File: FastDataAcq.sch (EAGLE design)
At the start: 224 parts, among them IC1 LT1963AEQ, IC2 FT230XQ, IC3 ADCMP553BRMZ, J1 MICRO-FIT_3.0_2POS_RA_SMD, J2 USB_MICROAB_SMT, X1 87832-14, X2 SMA-142-0701-801/806, X3 SMA-142-0701-801/806, Y1 SI530-500, Y2 100MHz, Y3 DNP

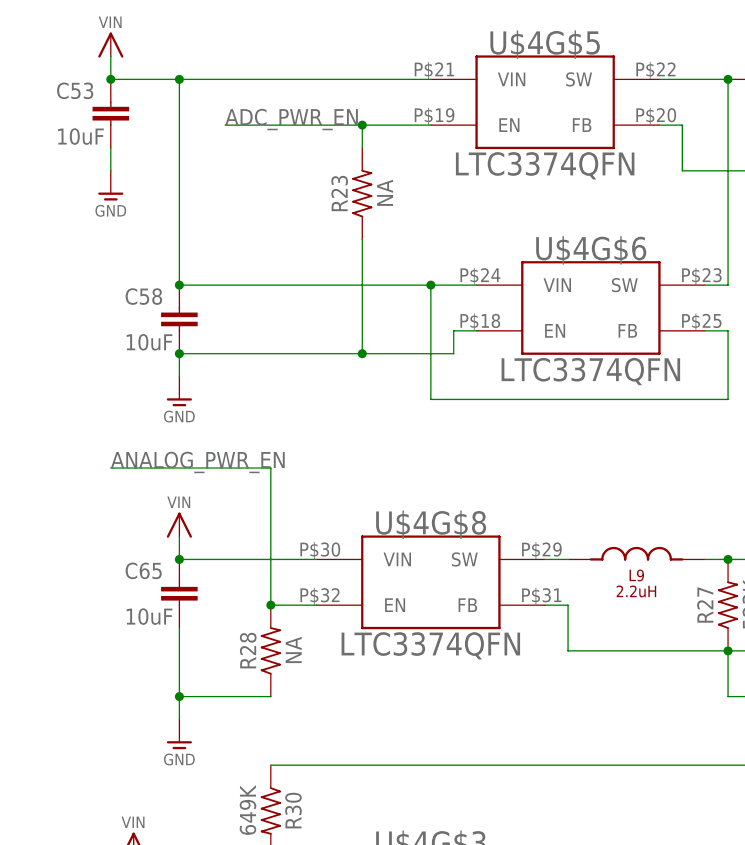
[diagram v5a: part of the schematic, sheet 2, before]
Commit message: Board layout almost complete.
Power plane almost routes all the power correctly.
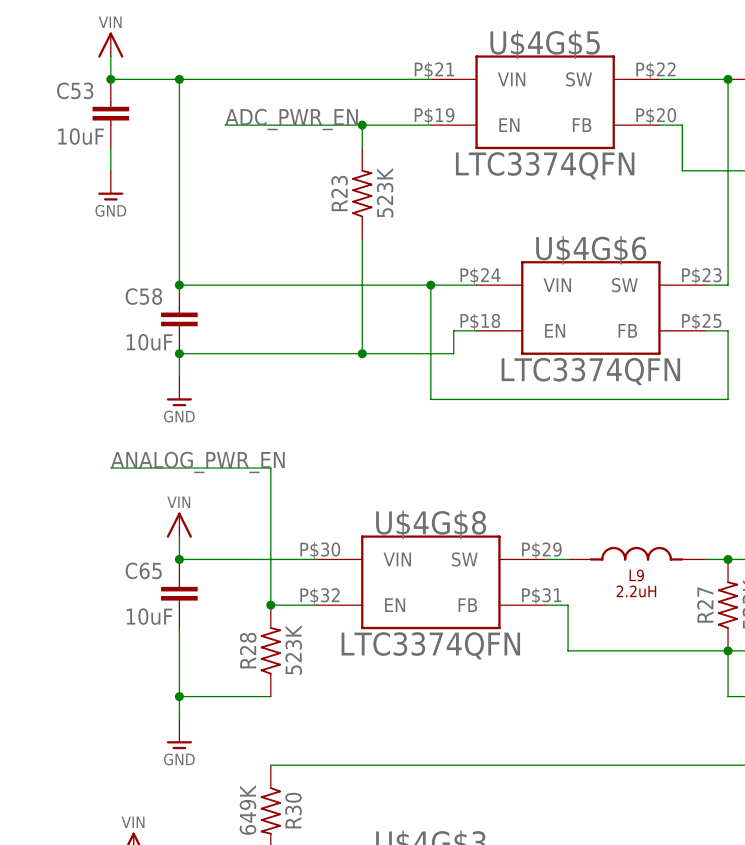
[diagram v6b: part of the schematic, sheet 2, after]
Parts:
- R23, R28: value NA -> 523K; device rcl:R-US_R0603 -> rcl:R-US_R0201; PARTNUMBER (none) -> P523KABCT-ND; SUPPLIER (none) -> DIGIKEY
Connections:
- net N$6 renamed S_MODE
- net S4EN renamed S3EN
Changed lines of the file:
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@@
 <attribute name="SUPPLIER" value=""/>
 </part>
-<part name="R28" library="rcl" deviceset="R-US_" device="R0603" value="NA">
-<attribute name="MANPARTNUMBER" value=""/>
-<attribute name="MANUFACTURER" value=""/>
-<attribute name="PARTNUMBER" value=""/>
-<attribute name="SUPPLIER" value=""/>
-</part>
-<part name="R23" library="rcl" deviceset="R-US_" device="R0603" value="NA">
-<attribute name="MANPARTNUMBER" value=""/>
-<attribute name="MANUFACTURER" value=""/>
-<attribute name="PARTNUMBER" value=""/>
-<attribute name="SUPPLIER" value=""/>
-</part>
 <part name="C7" library="rcl" deviceset="C-EU" device="C0603" value="NA">
 <attribute name="PARTNUMBER" value=""/>
@@
 <part name="S1" library="Schuyler" deviceset="SLIDER_SPDT" device="_AYZ0102AGRLC"/>
 <part name="SUPPLY1" library="Schuyler" deviceset="SUP_VIN" device="" value="Vin"/>
+<part name="R23" library="rcl" deviceset="R-US_" device="R0201" value="523K">
+<attribute name="PARTNUMBER" value="P523KABCT-ND"/>
+<attribute name="SUPPLIER" value="DIGIKEY"/>
+</part>
+<part name="R28" library="rcl" deviceset="R-US_" device="R0201" value="523K">
+<attribute name="PARTNUMBER" value="P523KABCT-ND"/>
+<attribute name="SUPPLIER" value="DIGIKEY"/>
+</part>
 </parts>
 <sheets>
@@
 <attribute name="SUPPLIER" x="22.86" y="17.78" size="1.778" layer="96" display="off"/>
 </instance>
-<instance part="R28" gate="G$1" x="33.02" y="50.8" rot="R90">
-<attribute name="MANPARTNUMBER" x="33.02" y="50.8" size="1.778" layer="96" rot="R90" display="off"/>
-<attribute name="MANUFACTURER" x="33.02" y="50.8" size="1.778" layer="96" rot="R90" display="off"/>
-<attribute name="PARTNUMBER" x="33.02" y="50.8" size="1.778" layer="96" rot="R90" display="off"/>
-<attribute name="SUPPLIER" x="33.02" y="50.8" size="1.778" layer="96" rot="R90" display="off"/>
-</instance>
-<instance part="R23" gate="G$1" x="43.18" y="101.6" rot="R90">
-<attribute name="MANPARTNUMBER" x="43.18" y="101.6" size="1.778" layer="96" rot="R90" display="off"/>
-<attribute name="MANUFACTURER" x="43.18" y="101.6" size="1.778" layer="96" rot="R90" display="off"/>
-<attribute name="PARTNUMBER" x="43.18" y="101.6" size="1.778" layer="96" rot="R90" display="off"/>
-<attribute name="SUPPLIER" x="43.18" y="101.6" size="1.778" layer="96" rot="R90" display="off"/>
-</instance>
 <instance part="C7" gate="G$1" x="157.48" y="210.82">
 <attribute name="PARTNUMBER" x="157.48" y="210.82" size="1.778" layer="96" display="off"/>
@@
 <instance part="S1" gate="G$1" x="25.4" y="193.04" rot="R90"/>
 <instance part="SUPPLY1" gate="G$1" x="43.18" y="203.2"/>
+<instance part="R23" gate="G$1" x="43.18" y="101.6" rot="R90">
+<attribute name="PARTNUMBER" x="43.18" y="101.6" size="1.778" layer="96" rot="R90" display="off"/>
+<attribute name="SUPPLIER" x="43.18" y="101.6" size="1.778" layer="96" rot="R90" display="off"/>
+</instance>
+<instance part="R28" gate="G$1" x="33.02" y="50.8" rot="R90">
+<attribute name="PARTNUMBER" x="33.02" y="50.8" size="1.778" layer="96" rot="R90" display="off"/>
+<attribute name="SUPPLIER" x="33.02" y="50.8" size="1.778" layer="96" rot="R90" display="off"/>
+</instance>
 </instances>
 <busses>
@@
 </segment>
 </net>
-<net name="N$6" class="0">
+<net name="S_MODE" class="0">
 <segment>
 <pinref part="U$4" gate="G$9" pin="MODE"/>
@@
 <wire x1="50.8" y1="109.22" x2="43.18" y2="109.22" width="0.1524" layer="91"/>
 <label x="27.94" y="109.22" size="1.778" layer="95"/>
-<pinref part="R23" gate="G$1" pin="2"/>
 <wire x1="43.18" y1="109.22" x2="27.94" y2="109.22" width="0.1524" layer="91"/>
 <wire x1="43.18" y1="106.68" x2="43.18" y2="109.22" width="0.1524" layer="91"/>
 <junction x="43.18" y="109.22"/>
+<pinref part="R23" gate="G$1" pin="2"/>
 </segment>
 </net>
@@
 </segment>
 </net>
-<net name="S4EN" class="0">
+<net name="S3EN" class="0">
 <segment>
 <pinref part="U$4" gate="G$3" pin="EN"/>
@@
 <pinref part="U$4" gate="G$6" pin="EN"/>
 <wire x1="53.34" y1="86.36" x2="55.88" y2="86.36" width="0.1524" layer="91"/>
-<pinref part="R23" gate="G$1" pin="1"/>
 <wire x1="43.18" y1="96.52" x2="43.18" y2="83.82" width="0.1524" layer="91"/>
 <junction x="43.18" y="83.82"/>
 <pinref part="U$61" gate="G$1" pin="GND"/>
+<pinref part="R23" gate="G$1" pin="1"/>
 </segment>
 <segment>
@@
 <wire x1="33.02" y1="45.72" x2="22.86" y2="45.72" width="0.1524" layer="91"/>
 <junction x="22.86" y="45.72"/>
-<pinref part="R28" gate="G$1" pin="1"/>
 <pinref part="U$63" gate="G$1" pin="GND"/>
+<pinref part="R28" gate="G$1" pin="1"/>
 </segment>
 <segment>

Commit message: Continued board layout
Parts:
- removed JP2: JUMPER-2PTH, SparkFun-Passives:JUMPER-2PTH
- removed JP3: M10", SparkFun-Connectors:M10"
- added J3: HEADER_0.1"_10P_2R_SMT, Schuyler:HEADER_0.1"_10P_2R_SMT
- added R40: 0, rcl:R-US_R0603
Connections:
- net 3V3: now also J3.P$1; no longer JP3.10
- net FPGA_GPIO1: now also J3.P$9; no longer JP3.2
- net FPGA_GPIO2: now also J3.P$8; no longer JP3.3
- net FPGA_GPIO3: now also J3.P$7; no longer JP3.4
- net FPGA_GPIO4: now also J3.P$6; no longer JP3.5
- net FPGA_GPIO5: now also J3.P$5; no longer JP3.6
- net FPGA_GPIO6: now also J3.P$4; no longer JP3.7
- net FPGA_GPIO7: now also J3.P$3; no longer JP3.8
- net GND: now also J3.P$2; no longer JP3.9
- net S_MODE: now also R40.2; no longer JP2.1
- net VIN: now also R40.1; no longer JP2.2
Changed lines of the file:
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@@
 <part name="TP3" library="testpad" deviceset="TP" device="PAD1-13"/>
 <part name="SUPPLY53" library="Schuyler" deviceset="SUP_VIN" device="" value="Vin"/>
-<part name="JP2" library="SparkFun-Passives" deviceset="JUMPER-2" device="PTH"/>
 <part name="SUPPLY74" library="Schuyler" deviceset="SUP_VIN" device="" value="Vin"/>
 <part name="R7" library="rcl" deviceset="R-US_" device="R0201" value="4.7k">
@@
 <part name="D3" library="Schuyler" deviceset="LED_" device="0603_GREEN"/>
 <part name="D4" library="Schuyler" deviceset="LED_" device="0603_RED"/>
-<part name="JP3" library="SparkFun-Connectors" deviceset="M10" device="&quot;"/>
 <part name="R42" library="rcl" deviceset="R-US_" device="R0201" value="330">
 <attribute name="MANPARTNUMBER" value="RC0603J331CS"/>
@@
 <attribute name="SUPPLIER" value="DIGIKEY"/>
 </part>
+<part name="R40" library="rcl" deviceset="R-US_" device="R0603" value="0">
+<attribute name="PARTNUMBER" value="311-0.0GRCT-ND"/>
+<attribute name="SUPPLIER" value="DIGIKEY"/>
+</part>
+<part name="J3" library="Schuyler" deviceset="HEADER_0.1&quot;_" device="10P_2R_SMT"/>
 </parts>
 <sheets>
@@
 <instance part="TP3" gate="G$1" x="251.46" y="223.52"/>
 <instance part="SUPPLY53" gate="G$1" x="109.22" y="220.98"/>
-<instance part="JP2" gate="A" x="116.84" y="228.6"/>
-<instance part="SUPPLY74" gate="G$1" x="124.46" y="228.6"/>
+<instance part="SUPPLY74" gate="G$1" x="127" y="228.6"/>
 <instance part="IC1" gate="A" x="165.1" y="106.68">
 <attribute name="MANPARTNUMBER" x="165.1" y="106.68" size="1.778" layer="96" display="off"/>
@@
 <attribute name="SUPPLIER" x="33.02" y="50.8" size="1.778" layer="96" rot="R90" display="off"/>
 </instance>
+<instance part="R40" gate="G$1" x="121.92" y="226.06" rot="R180">
+<attribute name="PARTNUMBER" x="121.92" y="226.06" size="1.778" layer="96" rot="R180" align="bottom-right" display="off"/>
+<attribute name="SUPPLIER" x="121.92" y="226.06" size="1.778" layer="96" rot="R180" align="bottom-right" display="off"/>
+</instance>
 </instances>
 <busses>
@@
 </segment>
 <segment>
-<pinref part="JP2" gate="A" pin="2"/>
 <pinref part="SUPPLY74" gate="G$1" pin="VIN"/>
-<wire x1="119.38" y1="226.06" x2="124.46" y2="226.06" width="0.1524" layer="91"/>
-<wire x1="124.46" y1="226.06" x2="124.46" y2="228.6" width="0.1524" layer="91"/>
+<wire x1="127" y1="226.06" x2="127" y2="228.6" width="0.1524" layer="91"/>
+<pinref part="R40" gate="G$1" pin="1"/>
 </segment>
 <segment>
@@
 <segment>
 <pinref part="U$4" gate="G$9" pin="MODE"/>
-<pinref part="JP2" gate="A" pin="1"/>
 <wire x1="104.14" y1="226.06" x2="116.84" y2="226.06" width="0.1524" layer="91"/>
 <wire x1="116.84" y1="226.06" x2="116.84" y2="223.52" width="0.1524" layer="91"/>
-<junction x="116.84" y="226.06"/>
 <pinref part="R18" gate="G$1" pin="2"/>
+<pinref part="R40" gate="G$1" pin="2"/>
+<junction x="116.84" y="226.06"/>
 </segment>
 </net>
@@
 <instance part="D3" gate="G$1" x="228.6" y="152.4"/>
 <instance part="D4" gate="G$1" x="238.76" y="152.4"/>
-<instance part="JP3" gate="G$1" x="172.72" y="162.56"/>
 <instance part="R42" gate="G$1" x="218.44" y="165.1" rot="R270">
 <attribute name="MANPARTNUMBER" x="218.44" y="165.1" size="1.778" layer="96" rot="R270" display="off"/>
@@
 <instance part="U$88" gate="G$1" x="55.88" y="149.86"/>
 <instance part="U$89" gate="G$1" x="210.82" y="165.1"/>
+<instance part="J3" gate="G$1" x="175.26" y="154.94"/>
 </instances>
 <busses>
@@
 <wire x1="210.82" y1="172.72" x2="210.82" y2="170.18" width="0.1524" layer="91"/>
 <label x="210.82" y="170.18" size="1.778" layer="95"/>
-<pinref part="JP3" gate="G$1" pin="10"/>
 <wire x1="210.82" y1="170.18" x2="210.82" y2="167.64" width="0.1524" layer="91"/>
 <wire x1="210.82" y1="167.64" x2="182.88" y2="167.64" width="0.1524" layer="91"/>
@@
 <label x="182.88" y="167.64" size="1.778" layer="95"/>
 <pinref part="U$21" gate="G$1" pin="3V3"/>
+<pinref part="J3" gate="G$1" pin="P$1"/>
 </segment>
 </net>
@@
 <wire x1="218.44" y1="149.86" x2="205.74" y2="149.86" width="0.1524" layer="91"/>
 <wire x1="205.74" y1="149.86" x2="205.74" y2="162.56" width="0.1524" layer="91"/>
-<pinref part="JP3" gate="G$1" pin="8"/>
 <wire x1="205.74" y1="162.56" x2="182.88" y2="162.56" width="0.1524" layer="91"/>
 <label x="182.88" y="162.56" size="1.778" layer="95"/>
+<pinref part="J3" gate="G$1" pin="P$3"/>
 </segment>
 </net>
 <net name="FPGA_GPIO6" class="0">
 <segment>
-<pinref part="JP3" gate="G$1" pin="7"/>
 <wire x1="182.88" y1="160.02" x2="203.2" y2="160.02" width="0.1524" layer="91"/>
 <wire x1="203.2" y1="160.02" x2="203.2" y2="147.32" width="0.1524" layer="91"/>
@@
 <wire x1="228.6" y1="147.32" x2="228.6" y2="149.86" width="0.1524" layer="91"/>
 <label x="182.88" y="160.02" size="1.778" layer="95"/>
+<pinref part="J3" gate="G$1" pin="P$4"/>
 </segment>
 </net>
@@
 <wire x1="238.76" y1="144.78" x2="200.66" y2="144.78" width="0.1524" layer="91"/>
 <wire x1="200.66" y1="144.78" x2="200.66" y2="157.48" width="0.1524" layer="91"/>
-<pinref part="JP3" gate="G$1" pin="6"/>
 <wire x1="200.66" y1="157.48" x2="182.88" y2="157.48" width="0.1524" layer="91"/>
 <label x="182.88" y="157.48" size="1.778" layer="95"/>
+<pinref part="J3" gate="G$1" pin="P$5"/>
 </segment>
 </net>
 <net name="FPGA_GPIO4" class="0">
 <segment>
-<pinref part="JP3" gate="G$1" pin="5"/>
 <wire x1="182.88" y1="154.94" x2="195.58" y2="154.94" width="0.1524" layer="91"/>
 <label x="182.88" y="154.94" size="1.778" layer="95"/>
+<pinref part="J3" gate="G$1" pin="P$6"/>
 </segment>
 </net>
 <net name="FPGA_GPIO3" class="0">
 <segment>
-<pinref part="JP3" gate="G$1" pin="4"/>
 <wire x1="182.88" y1="152.4" x2="195.58" y2="152.4" width="0.1524" layer="91"/>
 <label x="182.88" y="152.4" size="1.778" layer="95"/>
+<pinref part="J3" gate="G$1" pin="P$7"/>
 </segment>
 </net>
 <net name="FPGA_GPIO2" class="0">
 <segment>
-<pinref part="JP3" gate="G$1" pin="3"/>
 <wire x1="182.88" y1="149.86" x2="195.58" y2="149.86" width="0.1524" layer="91"/>
 <label x="182.88" y="149.86" size="1.778" layer="95"/>
+<pinref part="J3" gate="G$1" pin="P$8"/>
 </segment>
 </net>
 <net name="FPGA_GPIO1" class="0">
 <segment>
-<pinref part="JP3" gate="G$1" pin="2"/>
 <wire x1="182.88" y1="147.32" x2="195.58" y2="147.32" width="0.1524" layer="91"/>
 <label x="182.88" y="147.32" size="1.778" layer="95"/>
+<pinref part="J3" gate="G$1" pin="P$9"/>
 </segment>
 </net>
@@
 </segment>
 <segment>
-<pinref part="JP3" gate="G$1" pin="9"/>
 <wire x1="182.88" y1="165.1" x2="210.82" y2="165.1" width="0.1524" layer="91"/>
 <label x="182.88" y="165.1" size="1.778" layer="95"/>
 <pinref part="U$89" gate="G$1" pin="GND"/>
+<pinref part="J3" gate="G$1" pin="P$2"/>
 </segment>
 </net>
